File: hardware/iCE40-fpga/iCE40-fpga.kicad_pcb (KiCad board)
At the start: 2 copper layers, 50 x 22.9 mm, 78 parts, among them J1 USB_B_Micro, J2 JST_PH, J3 Feather, Q1 DMP2045U, SW1 SW_Push, U1 MCP73831-2-OT, U2 TPD2S017, U3 AP2112K-3.3, U4 AT25SF081-SSHD-X, U5 AP2112K-1.2, U6 ICE40UP5K-SG48ITR, U7 93C46B, U8 FT2232H, X1 DSC6101CI1A

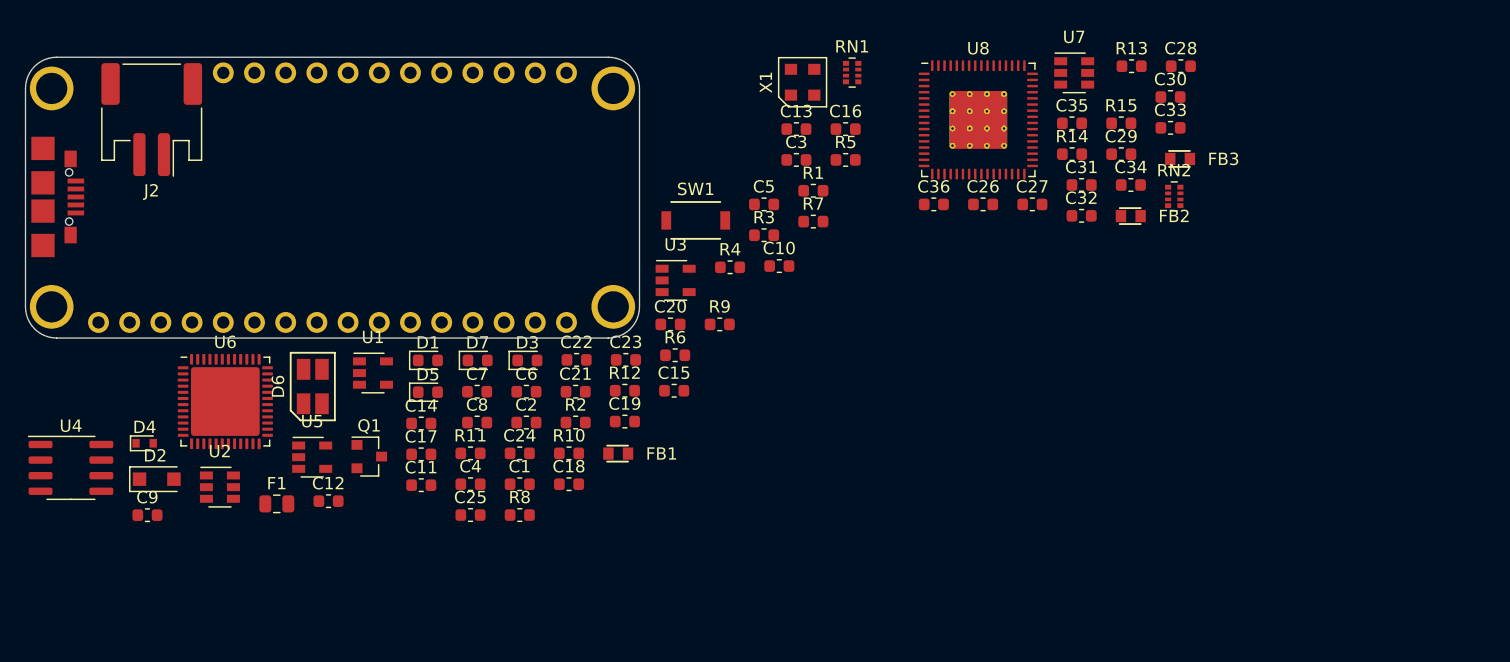
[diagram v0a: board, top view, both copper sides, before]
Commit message: fixed footprints + added extra feather headers
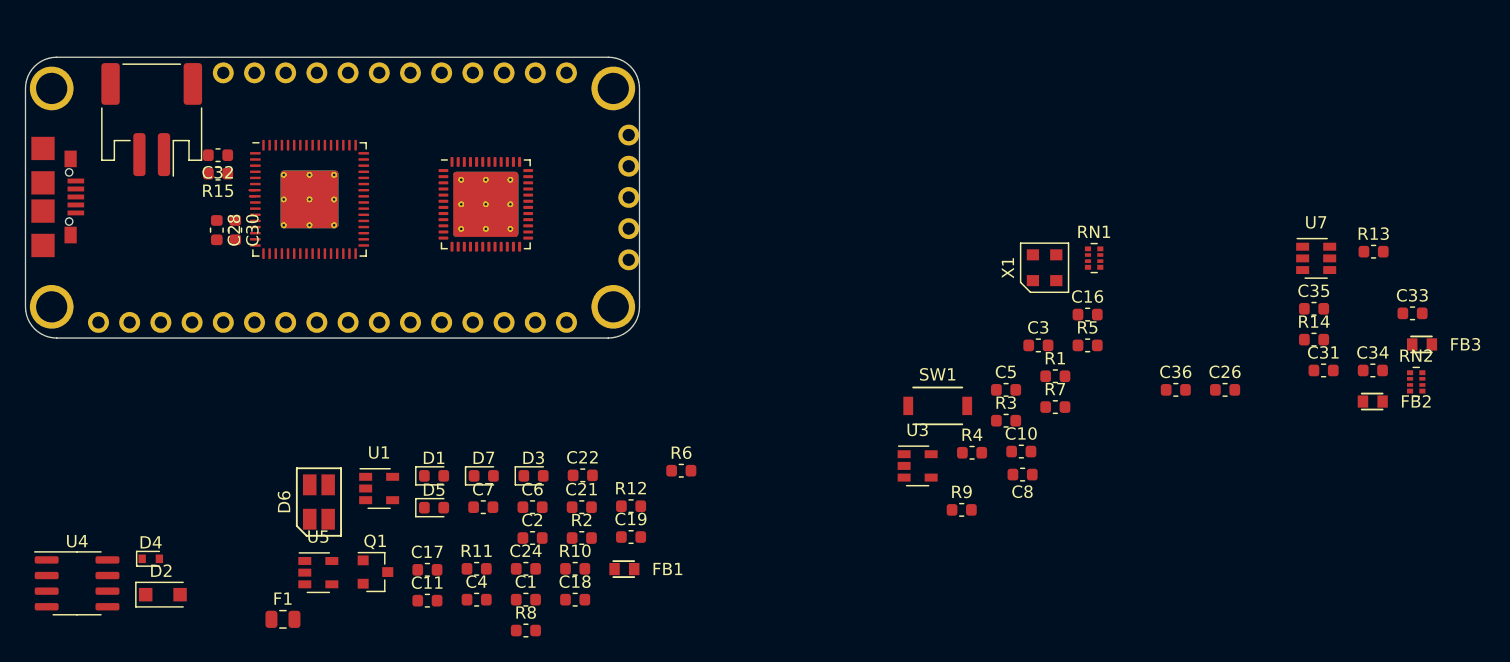
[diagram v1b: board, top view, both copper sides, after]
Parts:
- removed C12: 100n, Capacitor_SMD:C_0603_1608Metric
- removed C13, C20, C25, C9: 1u, Capacitor_SMD:C_0603_1608Metric
- removed C14, C15, C23: 10n, Capacitor_SMD:C_0603_1608Metric
- removed C27, C29: 4u7, Capacitor_SMD:C_0603_1608Metric
- removed U2: TPD2S017, Package_TO_SOT_SMD:SOT-23-6
- added J4: Bonus_Row, josh-footprints:PinSocket_1x05_P2.54mm_Vertical_No_Markings, F.Cu at (75.4, 33.8)
- C8: value 1u -> 100n
- U6: footprint Package_DFN_QFN:QFN-48-1EP_7x7mm_P0.5mm_EP5.6x5.6mm -> josh-footprints:QFN-48-1EP_7x7mm_P0.5mm_EP5.3x5.3mm_ThermalVias
- U8: footprint Package_DFN_QFN:QFN-64-1EP_9x9mm_P0.5mm_EP4.7x4.7mm_ThermalVias -> josh-footprints:QFN-64-1EP_9x9mm_P0.5mm_EP4.7x4.7mm_ThermalVias
- moved C28 79.6 mm to (41.9, 36.5), turned to 270 degrees
- moved C30 76.9 mm to (43.4, 36.5), turned to 270 degrees
- moved R15 73.6 mm to (42.0, 31.9), turned to 180 degrees
- moved C32 70.5 mm to (42.0, 30.4), turned to 180 degrees
- moved U8 54.8 mm to (49.5, 34.0)
- moved C8 44.6 mm to (107.5, 56.4), turned to 180 degrees
- moved U6 26.6 mm to (63.8, 34.4)
- moved C34 24.8 mm to (136.0, 47.9)
- moved RN2 24.8 mm to (139.5, 48.9)
- moved C16 24.8 mm to (112.8, 43.4)
- moved C26 24.8 mm to (124.0, 49.5)
- moved C33 24.8 mm to (139.2, 43.3)
- moved C36 24.8 mm to (120.0, 49.5)
- moved C5 24.8 mm to (106.2, 49.5)
- moved FB3 24.8 mm to (140.0, 45.8)
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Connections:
- C21 pad 1: Net-(C21-Pad1) -> +3V3
- D4 pad 2: Net-(C21-Pad1) -> +3V3
- J1 pad 2: Net-(J1-Pad2) -> /USB_N
- J1 pad 3: Net-(J1-Pad3) -> /USB_P
- U8 pad 7: /USB_DM -> /USB_N
- U8 pad 8: /USB_DP -> /USB_P
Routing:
- added copper zone on 3V3, net +3V3
- added copper zone on GND, net GND
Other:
- copper layers 2 -> 4
- net class Default: trace_width 0.25 -> 0.2; via_dia 0.8 -> 0.5; via_drill 0.4 -> 0.25
- rule trace_min: 0.2 -> 0.15
- rule via_min_drill: 0.3 -> 0.25
- rule via_min_size: 0.4 -> 0.5

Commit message: all nets routed
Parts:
- removed C17: 10u, Capacitor_SMD:C_0603_1608Metric
- removed D3: GRN, LED_SMD:LED_0603_1608Metric
- removed J4: Bonus_Row, josh-footprints:PinSocket_1x05_P2.54mm_Vertical_No_Markings
- removed R10, R12, R9: 1K, Resistor_SMD:R_0603_1608Metric
- removed R11: 10K, Resistor_SMD:R_0603_1608Metric
- removed SW1: SW_Push, josh-footprints:Small_Tact_Switch
- removed U4: AT25SF081-SSHD-X, Package_SO:SOIC-8_3.9x4.9mm_P1.27mm
- added RN3: 1K, Resistor_SMD:R_Array_Convex_4x0402, F.Cu at (52.1, 41.5)
- added U2: W25Q32JVZP, josh-footprints:WSON-8-1EP_6x5mm_P1.27mm_EP3.4x4.3mm, F.Cu at (63.1, 27.3)
- D6: value LED_RGBA -> LTST-C19HE1WT; footprint josh-footprints:ARGB_PLCC4_1210_LED -> josh-footprints:0606LED
- R5: value 2K2 -> 10K
- moved FB3 91.9 mm to (49.6, 29.2), turned to 90 degrees
- moved FB2 91.6 mm to (45.5, 36.1), turned to 180 degrees
- moved R13 87.3 mm to (49.6, 26.2), turned to 90 degrees
- moved RN2 86.3 mm to (56.2, 26.4)
- moved R14 85.0 mm to (46.5, 38.6), turned to 270 degrees
- moved C31 84.0 mm to (48.8, 36.1), turned to 180 degrees
- moved C33 83.3 mm to (57.3, 28.4), turned to 180 degrees
- moved U7 79.5 mm to (52.6, 27.8)
- moved C35 76.5 mm to (54.8, 41.8), turned to 180 degrees
- moved C26 75.4 mm to (52.6, 25.4), turned to 180 degrees
- moved R1 74.9 mm to (35.6, 41.4)
- moved C34 73.3 mm to (63.6, 36.6), turned to 180 degrees
- moved R5 67.3 mm to (45.7, 41.2), turned to 180 degrees
- moved R3 67.2 mm to (43.4, 27.9), turned to 180 degrees
- moved R7 66.4 mm to (44.9, 38.6), turned to 270 degrees
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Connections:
- J3 pad 10: (no net) -> /IO5
- J3 pad 11: (no net) -> /IO6
- J3 pad 12: (no net) -> /IO7
- J3 pad 13: (no net) -> /IO8
- J3 pad 14: (no net) -> /IO9
- J3 pad 15: (no net) -> /IO10
- J3 pad 17: (no net) -> /IO11
- J3 pad 18: (no net) -> /IO12
- J3 pad 19: (no net) -> /IO13
- J3 pad 20: (no net) -> /IO14
- J3 pad 21: (no net) -> /IO15
- J3 pad 22: (no net) -> /IO16
- J3 pad 23: (no net) -> /IO17
- J3 pad 24: (no net) -> /IO18
- J3 pad 25: (no net) -> /IO19
- J3 pad 5: (no net) -> /IO0
- J3 pad 6: (no net) -> /IO1
- J3 pad 7: (no net) -> /IO2
- J3 pad 8: (no net) -> /IO3
- J3 pad 9: (no net) -> /IO4
- R5 pad 1: Net-(D3-Pad2) -> +3V3
- R5 pad 2: +3V3 -> /nICE_CRESET
- R8 pad 1: (no net) -> /nLED
- RN1 pad 1: /ICE_SS -> /ICE_SCK
- RN1 pad 2: /ICE_SCK -> (no net)
- RN1 pad 4: /FLASH_nHOLD|IO3 -> /ICE_SS
- RN2 pad 1: /FTDI Programmer / UART/FT_EECS -> (no net)
- RN2 pad 2: /FTDI Programmer / UART/FT_EECLK -> /FTDI Programmer / UART/FT_EECS
- RN2 pad 3: /FTDI Programmer / UART/FT_EEDATA -> /FTDI Programmer / UART/FT_EECLK
- RN2 pad 4: (no net) -> /FTDI Programmer / UART/FT_EEDATA
- U6 pad 10: (no net) -> /IO17
- U6 pad 11: (no net) -> /IO18
- U6 pad 12: (no net) -> /IO19
- U6 pad 14: (no net) -> /FLASH_MOSI|IO0
- U6 pad 15: (no net) -> /ICE_SCK
- U6 pad 16: (no net) -> /ICE_SS
- U6 pad 17: (no net) -> /FLASH_MISO|IO1
- U6 pad 2: (no net) -> /IO12
- U6 pad 21: (no net) -> /TX_FPGA
- U6 pad 23: (no net) -> /RX_FPGA
- U6 pad 25: (no net) -> /IO0
- U6 pad 26: (no net) -> /IO1
- U6 pad 27: (no net) -> /IO2
- U6 pad 28: (no net) -> /IO3
- U6 pad 3: (no net) -> /IO13
- U6 pad 31: (no net) -> /IO4
- U6 pad 32: (no net) -> /IO5
- U6 pad 36: (no net) -> /IO6
- U6 pad 37: (no net) -> /IO7
- U6 pad 4: (no net) -> /IO14
- U6 pad 43: (no net) -> /IO8
- U6 pad 44: (no net) -> /IO10
- U6 pad 45: (no net) -> /IO9
- U6 pad 47: (no net) -> /nLED
- U6 pad 48: (no net) -> /IO11
- U6 pad 6: (no net) -> /IO15
- U6 pad 9: (no net) -> /IO16
- U8 pad 24: (no net) -> /nICE_CRESET
- U8 pad 38: (no net) -> /RX_FPGA
- U8 pad 39: (no net) -> /TX_FPGA
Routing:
- net +3V3: track 0.00 -> 69.0 mm, vias 0 -> 16
- net +1V2: track 0.00 -> 65.0 mm, vias 0 -> 5
- net /nICE_CRESET: track 0.00 -> 50.2 mm, vias 0 -> 5
- net /nLED: track 0.00 -> 49.8 mm, vias 0 -> 3
- net GND: track 0.00 -> 48.0 mm, vias 0 -> 54
- net +5V: track 0.00 -> 41.4 mm, vias 0 -> 2
- net /ICE_CDONE: track 0.00 -> 38.7 mm, vias 0 -> 5
- net /FLASH_MISO|IO1: track 0.00 -> 31.4 mm, vias 0 -> 2
- net /nLED_RED: track 0.00 -> 30.4 mm, vias 0 -> 2
- net +1V8: track 0.00 -> 30.2 mm, vias 0 -> 2
- net /FLASH_MOSI|IO0: track 0.00 -> 29.4 mm, vias 0 -> 3
- net /ICE_SCK: track 0.00 -> 29.3 mm, vias 0 -> 4
- net /nLED_GREEN: track 0.00 -> 29.1 mm, vias 0 -> 2
- net /IO0: track 0.00 -> 28.1 mm, vias 0 -> 1
- net /ICE_SS: track 0.00 -> 27.8 mm, vias 0 -> 4
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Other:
- net class Default: clearance 0.2 -> 0.15; trace_width 0.2 -> 0.15
- net class Power added: clearance 0.2, trace_width 0.3, via_dia 0.6, via_drill 0.3
- rule trace_clearance: 0.2 -> 0.15
- board text added: "CDONE"
- board text added: "CHG"
- board text added: "USR"

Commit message: cleaned up routing
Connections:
- U6 pad 31: /IO4 -> /IO5
- U6 pad 32: /IO5 -> /IO8
- U6 pad 36: /IO6 -> /IO9
- U6 pad 37: /IO7 -> /IO6
- U6 pad 43: /IO8 -> /IO4
- U6 pad 45: /IO9 -> /IO7
- U6 pad 47: /nLED -> /IO11
- U6 pad 48: /IO11 -> /nLED
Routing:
- net /IO4: track 21.9 -> 30.3 mm, vias 1 -> 2
- net /IO8: track 20.0 -> 12.4 mm, vias 2 -> 1
- net /IO7: track 17.9 -> 25.2 mm, vias 2 -> 1
- net /ICE_SS: track 27.8 -> 34.7 mm
- net /IO9: track 17.6 -> 11.3 mm
- net /nLED: track 49.8 -> 48.2 mm
- net /IO6: track 18.9 -> 20.4 mm, vias 2 -> 1
- net /IO11: track 9.67 -> 11.0 mm
- net /IO10: track 17.0 -> 15.8 mm
- net /nLED_GREEN: track 29.1 -> 30.1 mm
- net /nLED_BLUE: track 27.4 -> 28.3 mm
- net +1V2: track 65.0 -> 64.3 mm
- net /IO18: track 19.5 -> 18.8 mm
- net /FLASH_MOSI|IO0: track 29.4 -> 28.8 mm
- net /IO17: track 17.7 -> 17.0 mm
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
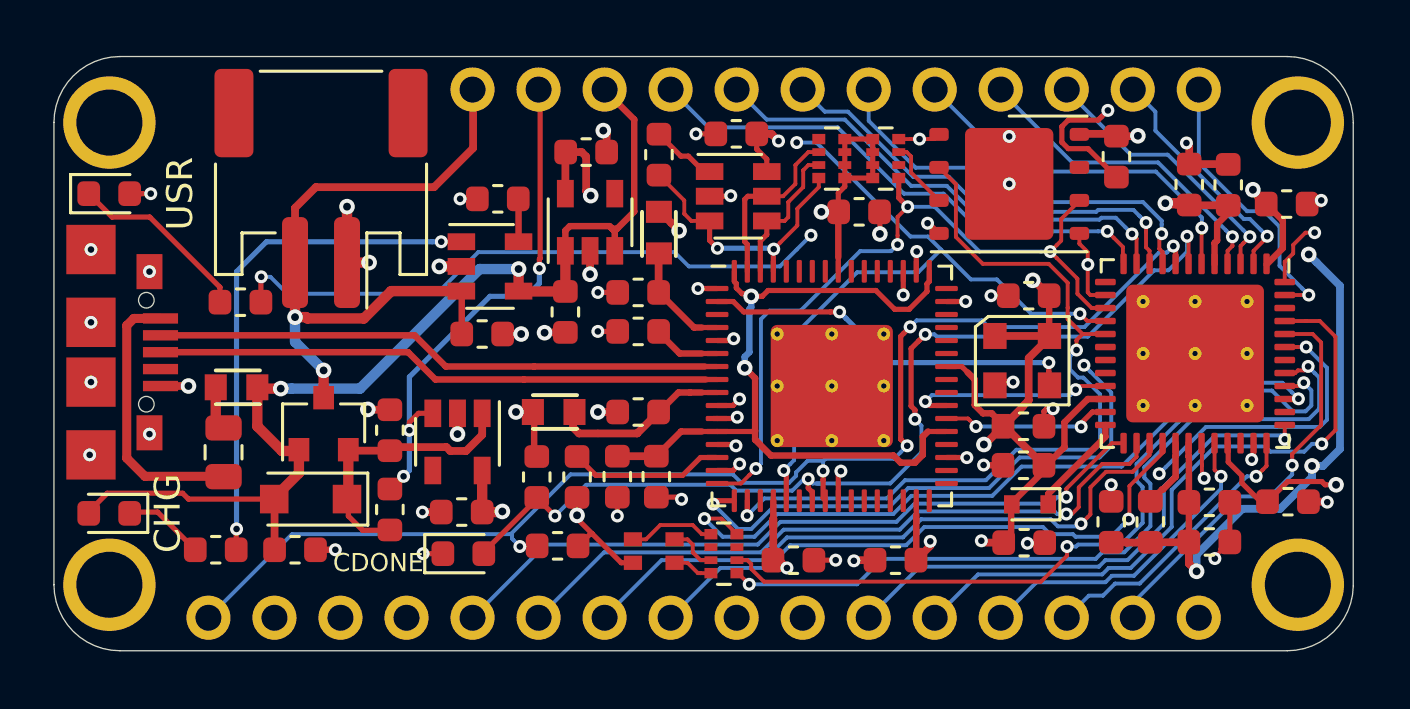
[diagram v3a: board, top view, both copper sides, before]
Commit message: added tx, rx leds, 7 segment and pmod wings
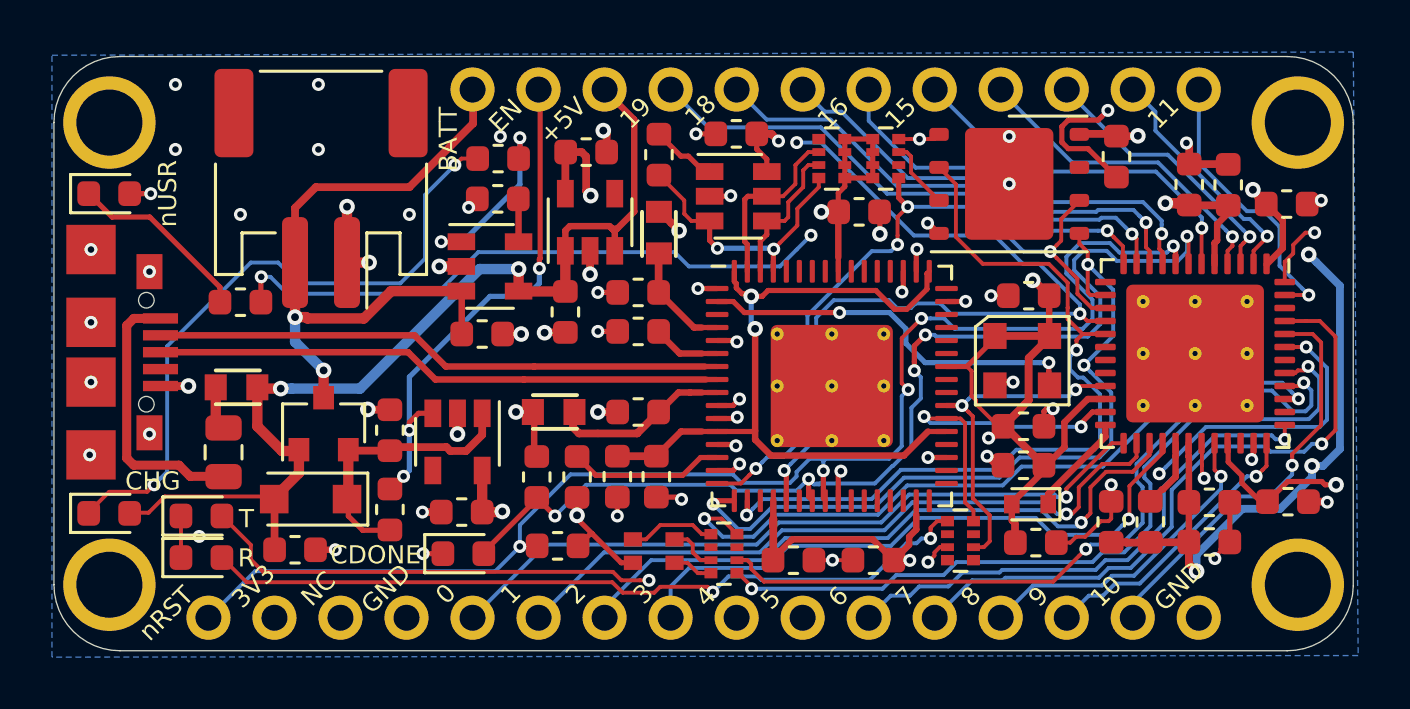
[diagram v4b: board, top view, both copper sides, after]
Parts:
- added D3: GRN, LED_SMD:LED_0603_1608Metric, F.Cu at (32.0, 41.7)
- added D8: GRN, LED_SMD:LED_0603_1608Metric, F.Cu at (32.0, 40.1)
- added REF**: KiCAD Logo, Symbol:Symbol_KiCAD-Logo_CopperAndSilkScreenTop, B.Cu at (33.3, 38.6)
- added REF**: Josh Details, josh-footprints:JoshDetails, B.Cu at (66.7, 40.1)
- added RN4: 330R, Resistor_SMD:R_Array_Convex_4x0402, F.Cu at (61.2, 41.0)
- RN3: value 1K -> 330R
- moved R2 18.6 mm to (43.4, 26.4)
- moved C36 0.85 mm to (57.9, 41.8)
- moved C21 0.45 mm to (64.1, 41.1)
- turned D1 to 0 degrees
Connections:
- U8 pad 65: (no net) -> GND
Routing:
- net Net-(D3-Pad2): track 0.00 -> 30.1 mm, vias 0 -> 2
- net Net-(D8-Pad2): track 0.00 -> 29.9 mm, vias 0 -> 2
- net Net-(D1-Pad1): track 3.12 -> 25.6 mm, vias 0 -> 2
- net Net-(R2-Pad1): track 19.8 -> 7.33 mm
- net +3V3: track 68.4 -> 76.4 mm, vias 16 -> 14
- net /RX_FPGA: track 6.56 -> 13.0 mm
- net /ICE_SS: track 34.7 -> 39.7 mm
- net /TX_FPGA: track 8.05 -> 12.8 mm
- net GND: track 48.2 -> 52.3 mm, vias 54 -> 60
- net /nICE_CRESET: track 50.0 -> 53.1 mm
- net /ICE_CDONE: track 38.7 -> 41.4 mm
- net +5V: track 41.4 -> 39.6 mm
- net /IO4: track 30.3 -> 31.8 mm
- net /IO3: track 23.0 -> 24.1 mm
- net +1V8: track 30.0 -> 28.9 mm
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- added copper zone on B.Cu, net GND
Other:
- board text added: "+5V"
- board text added: "0"
- board text added: "1"
- board text added: "10"
- board text added: "11"
- board text added: "15"
- board text added: "16"
- board text added: "18"
- board text added: "19"
- board text added: "2"
- board text added: "3"
- board text added: "3V3"
- board text added: "4"
- board text added: "5"
- board text added: "6"
- board text added: "7"
- board text added: "8"
- board text added: "9"
- board text added: "BATT"
- board text added: "EN"
- board text added: "GND"
- board text added: "NC"
- board text added: "R"
- board text added: "T"
- board text added: "nRST"
- board text added: "nUSR"
- board text removed: "USR"

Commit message: updated board + pmod
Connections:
- net VBUS renamed Net-(F1-Pad2)
- RN1 pad 2: (no net) -> /FLASH_nWP|IO2
- RN1 pad 3: /FLASH_nWP|IO2 -> /FLASH_nHOLD|IO3
- U2 pad 7: (no net) -> /FLASH_nHOLD|IO3
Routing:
- net /FLASH_nHOLD|IO3: track 0.00 -> 11.3 mm, vias 0 -> 2
- net GND: track 52.3 -> 50.0 mm, vias 60 -> 59
